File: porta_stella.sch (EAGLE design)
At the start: 105 parts, among them CN4 MicroUSB, IC1 74LS00D, J1 PJ-393, T1 2N3904, T2 PN3906, T3 PN3906, T4 PN3906, T5 MMUN2133LT1G, U1 TPS61090RSAR, U2 MCP73871, X1 SSW-112-02-G-Q

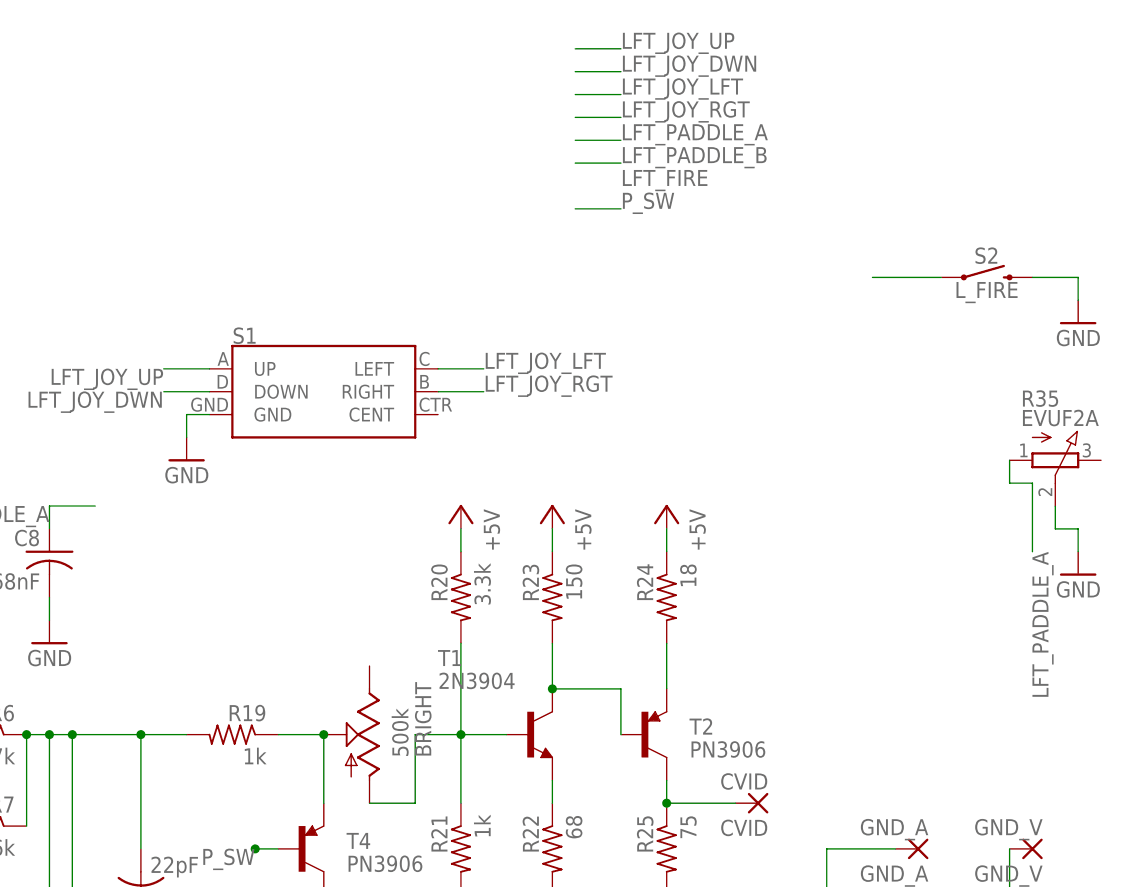
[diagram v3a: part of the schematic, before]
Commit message: resized again to make more room for the joystick
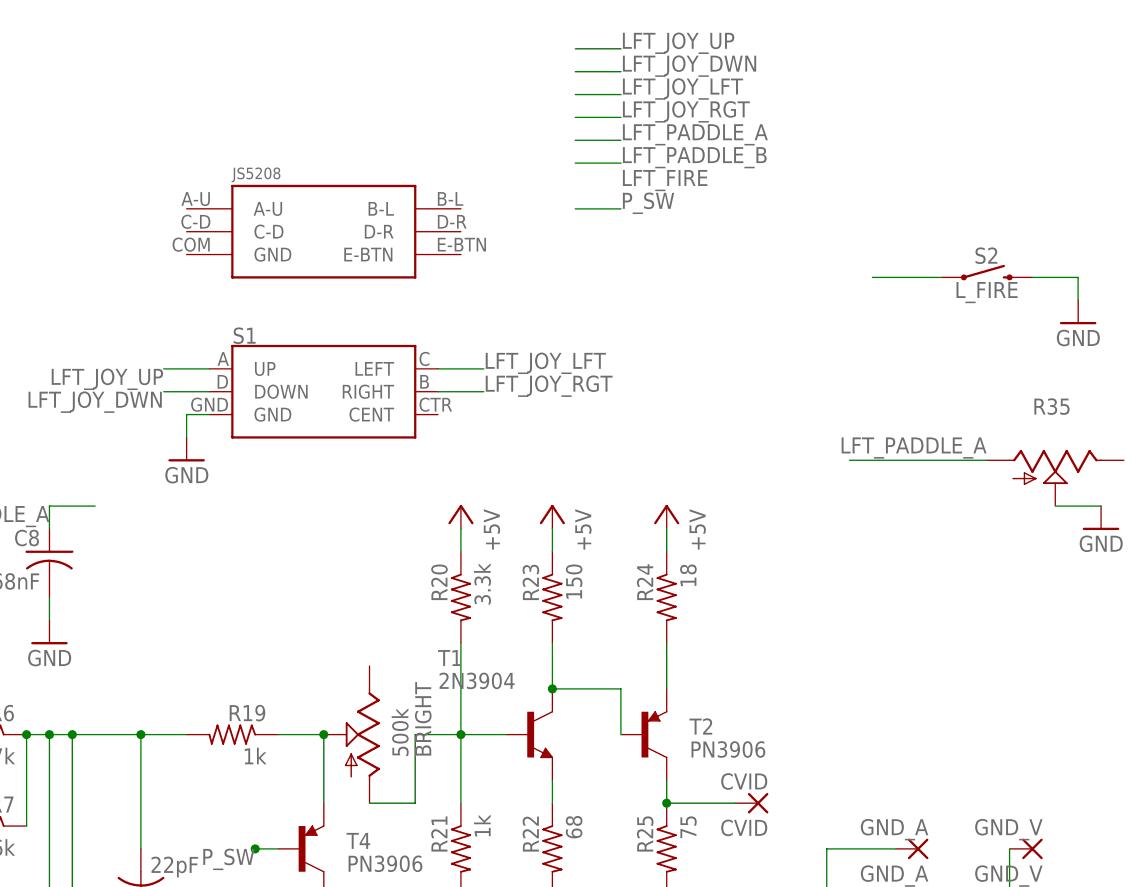
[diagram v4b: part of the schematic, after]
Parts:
- added U$5: JS5208, tiny_stella:JS5208
- R35: value EVUF2A -> (none); device pot:EVUF2A -> pot:TRIM_US-ECP10S
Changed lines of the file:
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@@
 <part name="CVID" library="wirepad" library_urn="urn:adsk.eagle:library:412" deviceset="WIREPAD" device="2,54/1,1" package3d_urn="urn:adsk.eagle:package:30836/1" value="CVID"/>
 <part name="GND3" library="supply1" library_urn="urn:adsk.eagle:library:371" deviceset="GND" device=""/>
-<part name="R35" library="pot" library_urn="urn:adsk.eagle:library:331" deviceset="EVU" device="A" package3d_urn="urn:adsk.eagle:package:22730/1" technology="F2"/>
+<part name="R35" library="pot" library_urn="urn:adsk.eagle:library:331" deviceset="TRIM_US-" device="ECP10S" package3d_urn="urn:adsk.eagle:package:22696/1"/>
 <part name="GND_A" library="wirepad" library_urn="urn:adsk.eagle:library:412" deviceset="WIREPAD" device="2,54/1,1" package3d_urn="urn:adsk.eagle:package:30836/1" value="GND_A"/>
 <part name="GND_V" library="wirepad" library_urn="urn:adsk.eagle:library:412" deviceset="WIREPAD" device="2,54/1,1" package3d_urn="urn:adsk.eagle:package:30836/1" value="GND_V"/>
@@
 <part name="ON/OFF1" library="special" library_urn="urn:adsk.eagle:library:367" deviceset="SW_DIP-1" device="" package3d_urn="urn:adsk.eagle:package:26661/1" value="ON/OFF"/>
 <part name="J1" library="Seeed-Connector" library_urn="urn:adsk.eagle:library:478" deviceset="AUDIO-JACK-PJ-393(8P-SMD)" device="" package3d_urn="urn:adsk.eagle:package:33126/1" value="PJ-393"/>
+<part name="U$5" library="tiny_stella" deviceset="JS5208" device=""/>
 </parts>
 <sheets>
@@
 <instance part="AUD" gate="G$1" x="208.28" y="7.62" rot="R90"/>
 <instance part="CVID" gate="G$1" x="312.42" y="60.96" rot="R180"/>
-<instance part="GND3" gate="1" x="347.98" y="86.36" rot="MR0"/>
+<instance part="GND3" gate="1" x="350.52" y="91.44" rot="MR0"/>
 <instance part="R35" gate="G$1" x="345.44" y="99.06" rot="R270"/>
 <instance part="GND_A" gate="G$1" x="330.2" y="55.88" rot="R180"/>
@@
 <instance part="ON/OFF1" gate="G$1" x="-154.94" y="73.66" rot="MR0"/>
 <instance part="J1" gate="G$1" x="312.42" y="17.78"/>
+<instance part="U$5" gate="G$1" x="264.16" y="124.46"/>
 </instances>
 <busses>
@@
 </segment>
 <segment>
-<wire x1="347.98" y1="91.44" x2="347.98" y2="88.9" width="0.1524" layer="91"/>
+<wire x1="345.44" y1="93.98" x2="350.52" y2="93.98" width="0.1524" layer="91"/>
 <pinref part="GND3" gate="1" pin="GND"/>
 <pinref part="R35" gate="G$1" pin="S"/>
-<wire x1="347.98" y1="91.44" x2="345.44" y2="91.44" width="0.1524" layer="91"/>
-<wire x1="345.44" y1="91.44" x2="345.44" y2="93.98" width="0.1524" layer="91"/>
 </segment>
 <segment>
@@
 </segment>
 <segment>
-<label x="342.9" y="88.9" size="1.778" layer="95" rot="R270"/>
-<wire x1="342.9" y1="88.9" x2="342.9" y2="96.52" width="0.1524" layer="91"/>
-<wire x1="342.9" y1="96.52" x2="340.36" y2="96.52" width="0.1524" layer="91"/>
+<label x="337.82" y="101.6" size="1.778" layer="95" rot="R180"/>
+<wire x1="322.58" y1="99.06" x2="337.82" y2="99.06" width="0.1524" layer="91"/>
 <pinref part="R35" gate="G$1" pin="A"/>
-<wire x1="340.36" y1="96.52" x2="340.36" y2="99.06" width="0.1524" layer="91"/>
-</segment>
-</net>
+</segment>
+</net>

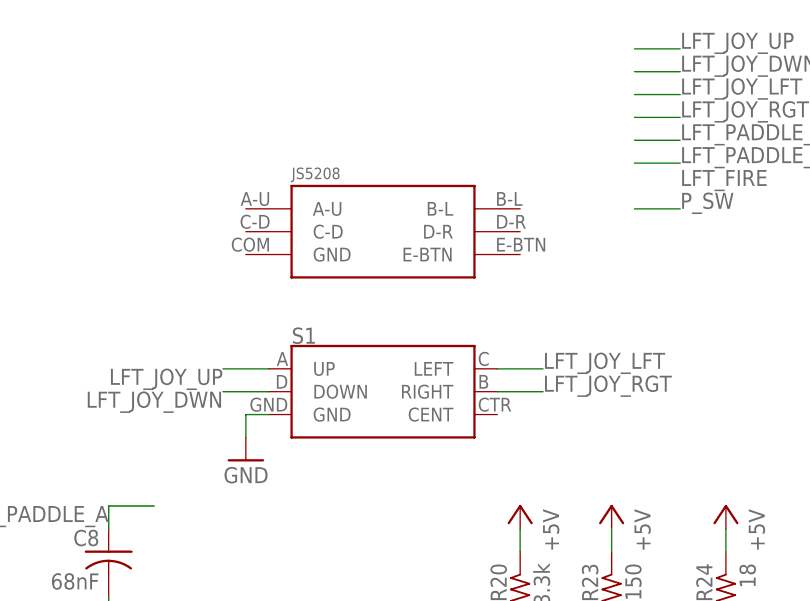
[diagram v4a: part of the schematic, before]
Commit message: switched to gameboy form factor
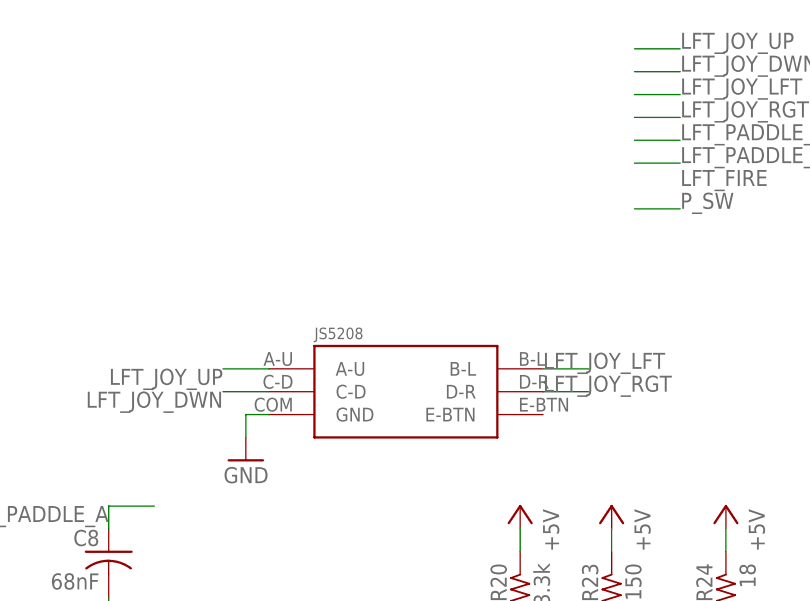
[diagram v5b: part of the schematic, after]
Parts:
- removed S1: (no value), SparkFun-Switches:JOYSTICK_MINI
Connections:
- net GND: now also U$5.GND; no longer S1.GND
- net LFT_JOY_DWN: now also U$5.C-D; no longer S1.DOWN
- net LFT_JOY_LFT: now also U$5.B-L; no longer S1.LEFT
- net LFT_JOY_RGT: now also U$5.D-R; no longer S1.RIGHT
- net LFT_JOY_UP: now also U$5.A-U; no longer S1.UP
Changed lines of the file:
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@@
 <part name="GND38" library="supply1" library_urn="urn:adsk.eagle:library:371" deviceset="GND" device=""/>
 <part name="T4" library="User-Submitted" library_urn="urn:adsk.eagle:library:536" deviceset="TRANSISTOR_PNP" device="PMBT3906" package3d_urn="urn:adsk.eagle:package:40256/1" value="PN3906"/>
-<part name="S1" library="SparkFun-Switches" library_urn="urn:adsk.eagle:library:535" deviceset="JOYSTICK_MINI" device="" package3d_urn="urn:adsk.eagle:package:40157/1"/>
 <part name="S2" library="SparkFun-Switches" library_urn="urn:adsk.eagle:library:535" deviceset="MOMENTARY-SWITCH-SPST" device="-SMD-5.2MM" package3d_urn="urn:adsk.eagle:package:40167/1" value="L_FIRE"/>
 <part name="GND6" library="supply1" library_urn="urn:adsk.eagle:library:371" deviceset="GND" device=""/>
@@
 <instance part="GND38" gate="1" x="264.16" y="33.02" rot="MR0"/>
 <instance part="T4" gate="G$1" x="261.62" y="55.88"/>
-<instance part="S1" gate="G$1" x="264.16" y="106.68"/>
 <instance part="S2" gate="G$1" x="337.82" y="119.38"/>
 <instance part="GND6" gate="1" x="248.92" y="99.06" rot="MR0"/>
@@
 <instance part="ON/OFF1" gate="G$1" x="-154.94" y="73.66" rot="MR0"/>
 <instance part="J1" gate="G$1" x="312.42" y="17.78"/>
-<instance part="U$5" gate="G$1" x="264.16" y="124.46"/>
+<instance part="U$5" gate="G$1" x="266.7" y="106.68"/>
 </instances>
 <busses>
@@
 </segment>
 <segment>
-<pinref part="S1" gate="G$1" pin="GND"/>
 <wire x1="251.46" y1="104.14" x2="248.92" y2="104.14" width="0.1524" layer="91"/>
 <pinref part="GND6" gate="1" pin="GND"/>
 <wire x1="248.92" y1="104.14" x2="248.92" y2="101.6" width="0.1524" layer="91"/>
+<pinref part="U$5" gate="G$1" pin="GND"/>
 </segment>
 <segment>
@@
 </segment>
 <segment>
-<wire x1="276.86" y1="106.68" x2="281.94" y2="106.68" width="0.1524" layer="91"/>
+<wire x1="287.02" y1="106.68" x2="281.94" y2="106.68" width="0.1524" layer="91"/>
 <label x="281.94" y="106.68" size="1.778" layer="95"/>
-<pinref part="S1" gate="G$1" pin="RIGHT"/>
+<pinref part="U$5" gate="G$1" pin="D-R"/>
 </segment>
 <segment>
@@
 </segment>
 <segment>
-<wire x1="276.86" y1="109.22" x2="281.94" y2="109.22" width="0.1524" layer="91"/>
+<wire x1="287.02" y1="109.22" x2="281.94" y2="109.22" width="0.1524" layer="91"/>
 <label x="281.94" y="109.22" size="1.778" layer="95"/>
-<pinref part="S1" gate="G$1" pin="LEFT"/>
+<pinref part="U$5" gate="G$1" pin="B-L"/>
 </segment>
 <segment>
@@
 <wire x1="251.46" y1="106.68" x2="246.38" y2="106.68" width="0.1524" layer="91"/>
 <label x="246.38" y="106.68" size="1.778" layer="95" rot="R180"/>
-<pinref part="S1" gate="G$1" pin="DOWN"/>
+<pinref part="U$5" gate="G$1" pin="C-D"/>
 </segment>
 <segment>
@@
 <wire x1="251.46" y1="109.22" x2="246.38" y2="109.22" width="0.1524" layer="91"/>
 <label x="246.38" y="109.22" size="1.778" layer="95" rot="R180"/>
-<pinref part="S1" gate="G$1" pin="UP"/>
-</segment>
-<segment>
+<pinref part="U$5" gate="G$1" pin="A-U"/>
+</segment>
+<segment>

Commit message: Added new switch
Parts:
- removed LDIFF: LFT_DIFFICULTY, special:SW_DIP-1
- removed ON/OFF1: ON/OFF, special:SW_DIP-1
- added L_DIFF, ON/OFF: JS202011JCQN, tiny_stella:JS202011JCQN
- PAUSE: value ON/OFF -> JS202011JCQN; device special:SW_DIP-1 -> tiny_stella:JS202011JCQN
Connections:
- net BOOST_ENABLE: now also ON/OFF.P$3, ON/OFF.P$6; no longer ON/OFF1.1
- net GND: now also L_DIFF.P$1, L_DIFF.P$2, L_DIFF.P$4, L_DIFF.P$5, ON/OFF.P$1, ON/OFF.P$2, ON/OFF.P$4, ON/OFF.P$5, PAUSE.P$1, PAUSE.P$2, PAUSE.P$4, PAUSE.P$5; no longer LDIFF.1, ON/OFF1.2, PAUSE.1
- net N$21: now also L_DIFF.P$3, L_DIFF.P$6; no longer LDIFF.2
- net P_SW: now also PAUSE.P$3, PAUSE.P$6; no longer PAUSE.2
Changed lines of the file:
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@@
 <part name="GND16" library="supply1" library_urn="urn:adsk.eagle:library:371" deviceset="GND" device=""/>
 <part name="JP1" library="SparkFun-Jumpers" library_urn="urn:adsk.eagle:library:528" deviceset="JUMPER-SMT_2_NO" device="_NO-SILK" package3d_urn="urn:adsk.eagle:package:39277/1" value="COLOR/BW"/>
-<part name="LDIFF" library="special" library_urn="urn:adsk.eagle:library:367" deviceset="SW_DIP-1" device="" package3d_urn="urn:adsk.eagle:package:26661/1" value="LFT_DIFFICULTY"/>
 <part name="GND17" library="supply1" library_urn="urn:adsk.eagle:library:371" deviceset="GND" device=""/>
 <part name="R18" library="resistor" library_urn="urn:adsk.eagle:library:348" deviceset="R-US_" device="M0805" package3d_urn="urn:adsk.eagle:package:26079/1" value="24k"/>
@@
 <part name="R33" library="resistor" library_urn="urn:adsk.eagle:library:348" deviceset="R-US_" device="M0805" package3d_urn="urn:adsk.eagle:package:26079/1" value="1k"/>
 <part name="R34" library="resistor" library_urn="urn:adsk.eagle:library:348" deviceset="R-US_" device="M0805" package3d_urn="urn:adsk.eagle:package:26079/1" value="1k"/>
-<part name="PAUSE" library="special" library_urn="urn:adsk.eagle:library:367" deviceset="SW_DIP-1" device="" package3d_urn="urn:adsk.eagle:package:26661/1" value="ON/OFF"/>
 <part name="D3" library="eagle-ltspice" library_urn="urn:adsk.eagle:library:217" deviceset="DIODE_E-" device="" package3d_urn="urn:adsk.eagle:package:13312/1"/>
 <part name="P+13" library="supply1" library_urn="urn:adsk.eagle:library:371" deviceset="+5V" device=""/>
@@
 <part name="U$25" library="microbuilder" deviceset="GND" device=""/>
 <part name="GND45" library="supply1" deviceset="GND" device=""/>
-<part name="ON/OFF1" library="special" library_urn="urn:adsk.eagle:library:367" deviceset="SW_DIP-1" device="" package3d_urn="urn:adsk.eagle:package:26661/1" value="ON/OFF"/>
 <part name="J1" library="Seeed-Connector" library_urn="urn:adsk.eagle:library:478" deviceset="AUDIO-JACK-PJ-393(8P-SMD)" device="" package3d_urn="urn:adsk.eagle:package:33126/1" value="PJ-393"/>
 <part name="U$5" library="tiny_stella" deviceset="JS5208" device=""/>
+<part name="PAUSE" library="tiny_stella" deviceset="JS202011JCQN" device=""/>
+<part name="ON/OFF" library="tiny_stella" deviceset="JS202011JCQN" device=""/>
+<part name="L_DIFF" library="tiny_stella" deviceset="JS202011JCQN" device=""/>
+<part name="GND2" library="supply1" library_urn="urn:adsk.eagle:library:371" deviceset="GND" device=""/>
 </parts>
 <sheets>
@@
 <instance part="GND16" gate="1" x="83.82" y="91.44"/>
 <instance part="JP1" gate="G$1" x="71.12" y="86.36"/>
-<instance part="LDIFF" gate="G$1" x="78.74" y="76.2" rot="MR180"/>
-<instance part="GND17" gate="1" x="93.98" y="71.12"/>
+<instance part="GND17" gate="1" x="93.98" y="78.74"/>
 <instance part="R18" gate="G$1" x="10.16" y="2.54" rot="MR0"/>
 <instance part="P+14" gate="1" x="15.24" y="7.62" rot="MR0"/>
@@
 <instance part="R33" gate="G$1" x="-88.9" y="124.46" rot="MR270"/>
 <instance part="R34" gate="G$1" x="-162.56" y="142.24" rot="MR270"/>
-<instance part="PAUSE" gate="G$1" x="-185.42" y="137.16" rot="MR0"/>
 <instance part="D3" gate="G$1" x="-149.86" y="137.16" rot="R270"/>
 <instance part="P+13" gate="1" x="-55.88" y="139.7"/>
@@
 <instance part="U2" gate="G$1" x="-208.28" y="-10.16"/>
 <instance part="C22" gate="G$1" x="-246.38" y="-66.04"/>
-<instance part="U$25" gate="G$1" x="-147.32" y="58.42"/>
+<instance part="U$25" gate="G$1" x="-152.4" y="35.56"/>
 <instance part="GND45" gate="1" x="-152.4" y="-50.8"/>
-<instance part="ON/OFF1" gate="G$1" x="-154.94" y="73.66" rot="MR0"/>
 <instance part="J1" gate="G$1" x="312.42" y="17.78"/>
 <instance part="U$5" gate="G$1" x="266.7" y="106.68"/>
+<instance part="PAUSE" gate="G$1" x="-187.96" y="154.94"/>
+<instance part="ON/OFF" gate="G$1" x="-152.4" y="58.42"/>
+<instance part="L_DIFF" gate="G$1" x="83.82" y="58.42" rot="R180"/>
+<instance part="GND2" gate="1" x="86.36" y="43.18"/>
 </instances>
 <busses>
@@
 <pinref part="JP1" gate="G$1" pin="2"/>
 <wire x1="76.2" y1="86.36" x2="93.98" y2="86.36" width="0.1524" layer="91"/>
-<pinref part="LDIFF" gate="G$1" pin="1"/>
-<wire x1="86.36" y1="76.2" x2="93.98" y2="76.2" width="0.1524" layer="91"/>
-<wire x1="93.98" y1="86.36" x2="93.98" y2="76.2" width="0.1524" layer="91"/>
-<wire x1="93.98" y1="76.2" x2="93.98" y2="73.66" width="0.1524" layer="91"/>
-<junction x="93.98" y="76.2"/>
+<wire x1="93.98" y1="86.36" x2="93.98" y2="81.28" width="0.1524" layer="91"/>
 <pinref part="GND17" gate="1" pin="GND"/>
 </segment>
@@
 </segment>
 <segment>
-<pinref part="PAUSE" gate="G$1" pin="1"/>
 <pinref part="GND35" gate="1" pin="GND"/>
-<wire x1="-193.04" y1="137.16" x2="-198.12" y2="137.16" width="0.1524" layer="91"/>
 <wire x1="-198.12" y1="137.16" x2="-198.12" y2="129.54" width="0.1524" layer="91"/>
+<wire x1="-198.12" y1="137.16" x2="-187.96" y2="137.16" width="0.1524" layer="91"/>
+<pinref part="PAUSE" gate="G$1" pin="P$5"/>
+<wire x1="-187.96" y1="137.16" x2="-187.96" y2="152.4" width="0.1524" layer="91"/>
+<pinref part="PAUSE" gate="G$1" pin="P$2"/>
+<wire x1="-187.96" y1="160.02" x2="-187.96" y2="152.4" width="0.1524" layer="91"/>
+<junction x="-187.96" y="152.4"/>
+<pinref part="PAUSE" gate="G$1" pin="P$4"/>
+<wire x1="-187.96" y1="152.4" x2="-195.58" y2="152.4" width="0.1524" layer="91"/>
+<pinref part="PAUSE" gate="G$1" pin="P$1"/>
+<wire x1="-187.96" y1="160.02" x2="-195.58" y2="160.02" width="0.1524" layer="91"/>
+<junction x="-187.96" y="160.02"/>
 </segment>
 <segment>
@@
 <segment>
 <pinref part="U$25" gate="G$1" pin="GND"/>
-<wire x1="-147.32" y1="73.66" x2="-147.32" y2="60.96" width="0.1524" layer="91"/>
-<pinref part="ON/OFF1" gate="G$1" pin="2"/>
+<pinref part="ON/OFF" gate="G$1" pin="P$5"/>
+<wire x1="-152.4" y1="55.88" x2="-152.4" y2="38.1" width="0.1524" layer="91"/>
+<pinref part="ON/OFF" gate="G$1" pin="P$4"/>
+<wire x1="-152.4" y1="55.88" x2="-160.02" y2="55.88" width="0.1524" layer="91"/>
+<junction x="-152.4" y="55.88"/>
+<pinref part="ON/OFF" gate="G$1" pin="P$1"/>
+<wire x1="-160.02" y1="63.5" x2="-160.02" y2="55.88" width="0.1524" layer="91"/>
+<junction x="-160.02" y="55.88"/>
+<pinref part="ON/OFF" gate="G$1" pin="P$2"/>
+<wire x1="-152.4" y1="63.5" x2="-152.4" y2="55.88" width="0.1524" layer="91"/>
 </segment>
 <segment>
 <wire x1="-152.4" y1="-33.02" x2="-152.4" y2="-48.26" width="0.1524" layer="91"/>
 <pinref part="GND45" gate="1" pin="GND"/>
+</segment>
+<segment>
+<pinref part="GND2" gate="1" pin="GND"/>
+<pinref part="L_DIFF" gate="G$1" pin="P$2"/>
+<wire x1="86.36" y1="45.72" x2="83.82" y2="45.72" width="0.1524" layer="91"/>
+<wire x1="83.82" y1="45.72" x2="83.82" y2="53.34" width="0.1524" layer="91"/>
+<wire x1="86.36" y1="45.72" x2="91.44" y2="45.72" width="0.1524" layer="91"/>
+<junction x="86.36" y="45.72"/>
+<pinref part="L_DIFF" gate="G$1" pin="P$1"/>
+<wire x1="91.44" y1="45.72" x2="91.44" y2="53.34" width="0.1524" layer="91"/>
+<pinref part="L_DIFF" gate="G$1" pin="P$4"/>
+<wire x1="91.44" y1="60.96" x2="91.44" y2="53.34" width="0.1524" layer="91"/>
+<junction x="91.44" y="53.34"/>
+<pinref part="L_DIFF" gate="G$1" pin="P$5"/>
+<wire x1="83.82" y1="60.96" x2="83.82" y2="53.34" width="0.1524" layer="91"/>
+<junction x="83.82" y="53.34"/>
 </segment>
 </net>
@@
 <wire x1="58.42" y1="53.34" x2="68.58" y2="53.34" width="0.1524" layer="91"/>
 <wire x1="68.58" y1="53.34" x2="68.58" y2="60.96" width="0.1524" layer="91"/>
-<pinref part="LDIFF" gate="G$1" pin="2"/>
-<wire x1="71.12" y1="76.2" x2="68.58" y2="76.2" width="0.1524" layer="91"/>
-<wire x1="68.58" y1="76.2" x2="68.58" y2="60.96" width="0.1524" layer="91"/>
+<pinref part="L_DIFF" gate="G$1" pin="P$6"/>
+<wire x1="76.2" y1="60.96" x2="68.58" y2="60.96" width="0.1524" layer="91"/>
+<pinref part="L_DIFF" gate="G$1" pin="P$3"/>
+<wire x1="76.2" y1="53.34" x2="68.58" y2="53.34" width="0.1524" layer="91"/>
+<junction x="68.58" y="53.34"/>
 </segment>
 </net>
@@
 <segment>
 <pinref part="R34" gate="G$1" pin="2"/>
-<pinref part="PAUSE" gate="G$1" pin="2"/>
-<wire x1="-162.56" y1="137.16" x2="-177.8" y2="137.16" width="0.1524" layer="91"/>
+<wire x1="-162.56" y1="137.16" x2="-180.34" y2="137.16" width="0.1524" layer="91"/>
 <label x="-170.18" y="137.16" size="1.778" layer="95" rot="R180"/>
 <pinref part="D3" gate="G$1" pin="A"/>
 <wire x1="-152.4" y1="137.16" x2="-162.56" y2="137.16" width="0.1524" layer="91"/>
 <junction x="-162.56" y="137.16"/>
+<pinref part="PAUSE" gate="G$1" pin="P$6"/>
+<wire x1="-180.34" y1="137.16" x2="-180.34" y2="152.4" width="0.1524" layer="91"/>
+<pinref part="PAUSE" gate="G$1" pin="P$3"/>
+<wire x1="-180.34" y1="152.4" x2="-180.34" y2="160.02" width="0.1524" layer="91"/>
+<junction x="-180.34" y="152.4"/>
 </segment>
 <segment>
@@
 </segment>
 <segment>
-<label x="-162.56" y="58.42" size="1.778" layer="95" rot="R270"/>
-<wire x1="-162.56" y1="58.42" x2="-162.56" y2="73.66" width="0.1524" layer="91"/>
-<pinref part="ON/OFF1" gate="G$1" pin="1"/>
-</segment>
-</net>
+<label x="-144.78" y="35.56" size="1.778" layer="95" rot="R270"/>
+<pinref part="ON/OFF" gate="G$1" pin="P$6"/>
+<wire x1="-144.78" y1="55.88" x2="-144.78" y2="35.56" width="0.1524" layer="91"/>
+<pinref part="ON/OFF" gate="G$1" pin="P$3"/>
+<wire x1="-144.78" y1="55.88" x2="-144.78" y2="63.5" width="0.1524" layer="91"/>
+<junction x="-144.78" y="55.88"/>
+</segment>
+</net>
